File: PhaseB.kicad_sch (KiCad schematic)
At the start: 12 parts, among them Q10 Q_NMOS, Q9 Q_NMOS, U2 STDriveG600

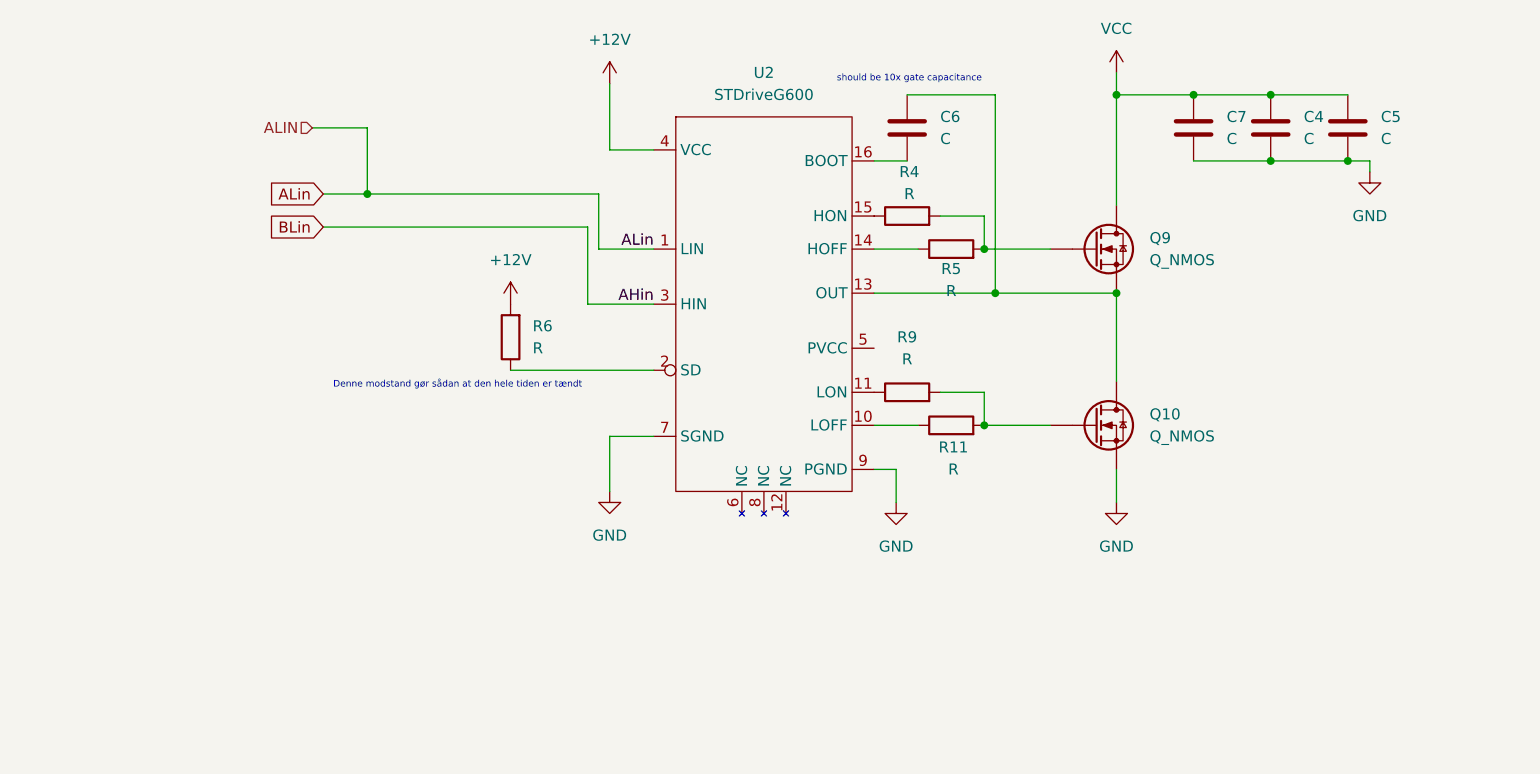
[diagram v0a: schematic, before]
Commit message: added hirearchical labels
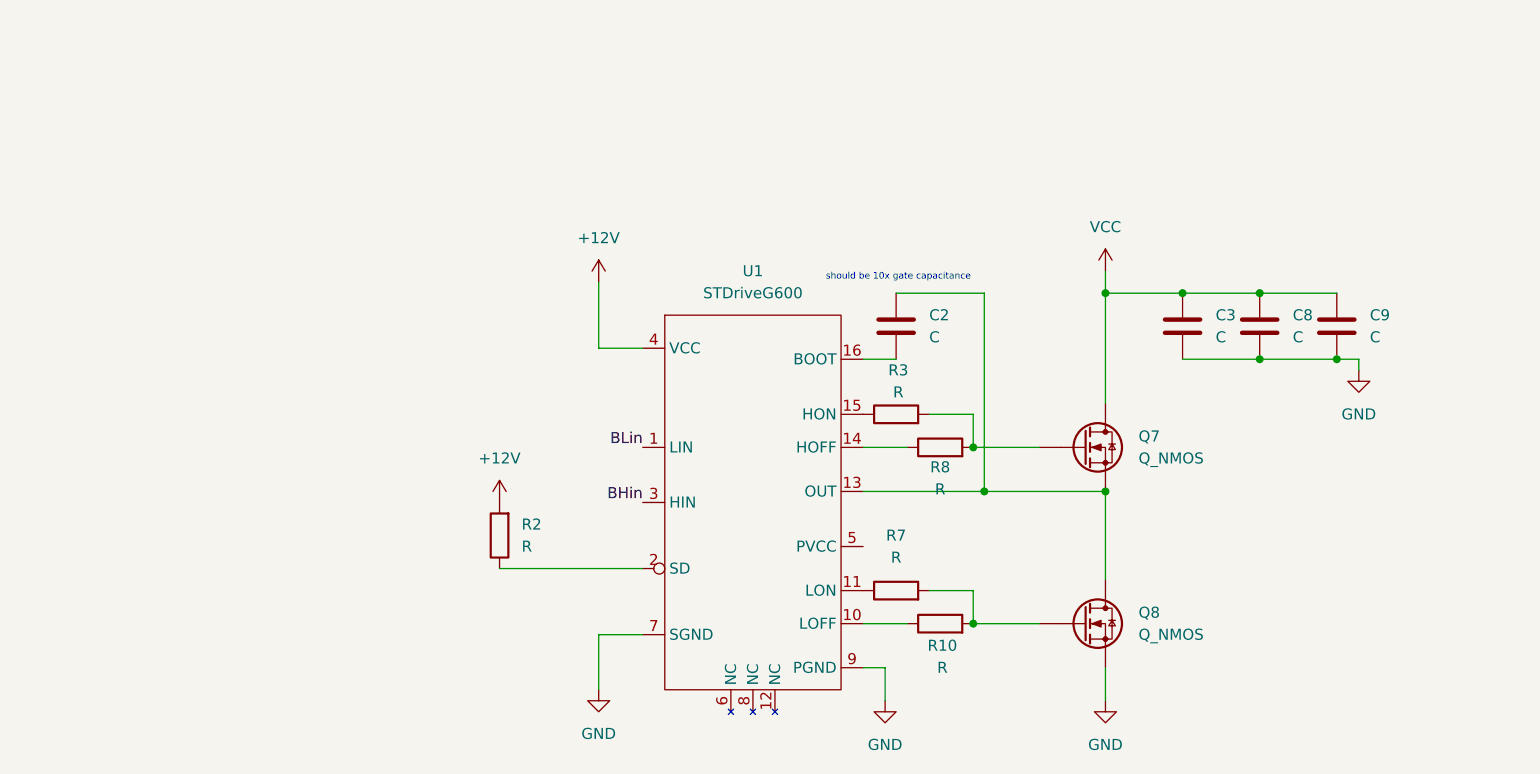
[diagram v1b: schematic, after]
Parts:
- removed C4, C5, C6, C7: C, symbol Device:C
- removed Q10, Q9: Q_NMOS, symbol Device:Q_NMOS
- removed R11, R4, R5, R6, R9: R, symbol Device:R
- removed U2: STDriveG600, Package_SO:SO-16_3.9x9.9mm_P1.27mm, symbol stm:STDRIVEG600
- added C2, C3, C8, C9: C, symbol Device:C
- added Q7, Q8: Q_NMOS, symbol Device:Q_NMOS
- added R10, R2, R3, R7, R8: R, symbol Device:R
- added U1: STDriveG600, Package_SO:SO-16_3.9x9.9mm_P1.27mm, symbol stm:STDRIVEG600
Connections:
- net +12V: now also R2.2, U1.4 (VCC)
- net BLin: now also U1.1 (LIN)
- net GND: now also C3.2, C8.2, C9.2, Q8.S, U1.7 (SGND), U1.9 (PGND)
- net VCC: now also C3.1, C8.1, C9.1, Q7.D
- new net: C2.1, Q7.S, Q8.D, U1.13 (OUT)
- new net: C2.2, U1.16 (BOOT)
- new net: R8.1, U1.14 (HOFF)
- new net: Q7.G, R3.2, R8.2
- new net: R10.1, U1.10 (LOFF)
- new net: R7.1, U1.11 (LON)
- new net: R3.1, U1.15 (HON)
- new net: R2.1, U1.2 (SD)
- new net: Q8.G, R10.2, R7.2
- new net BHin: U1.3 (HIN)
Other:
- note removed: "Denne modstand gør sådan at den hele tiden er tændt"

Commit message: added more data for the 3 Phases. also added transformer
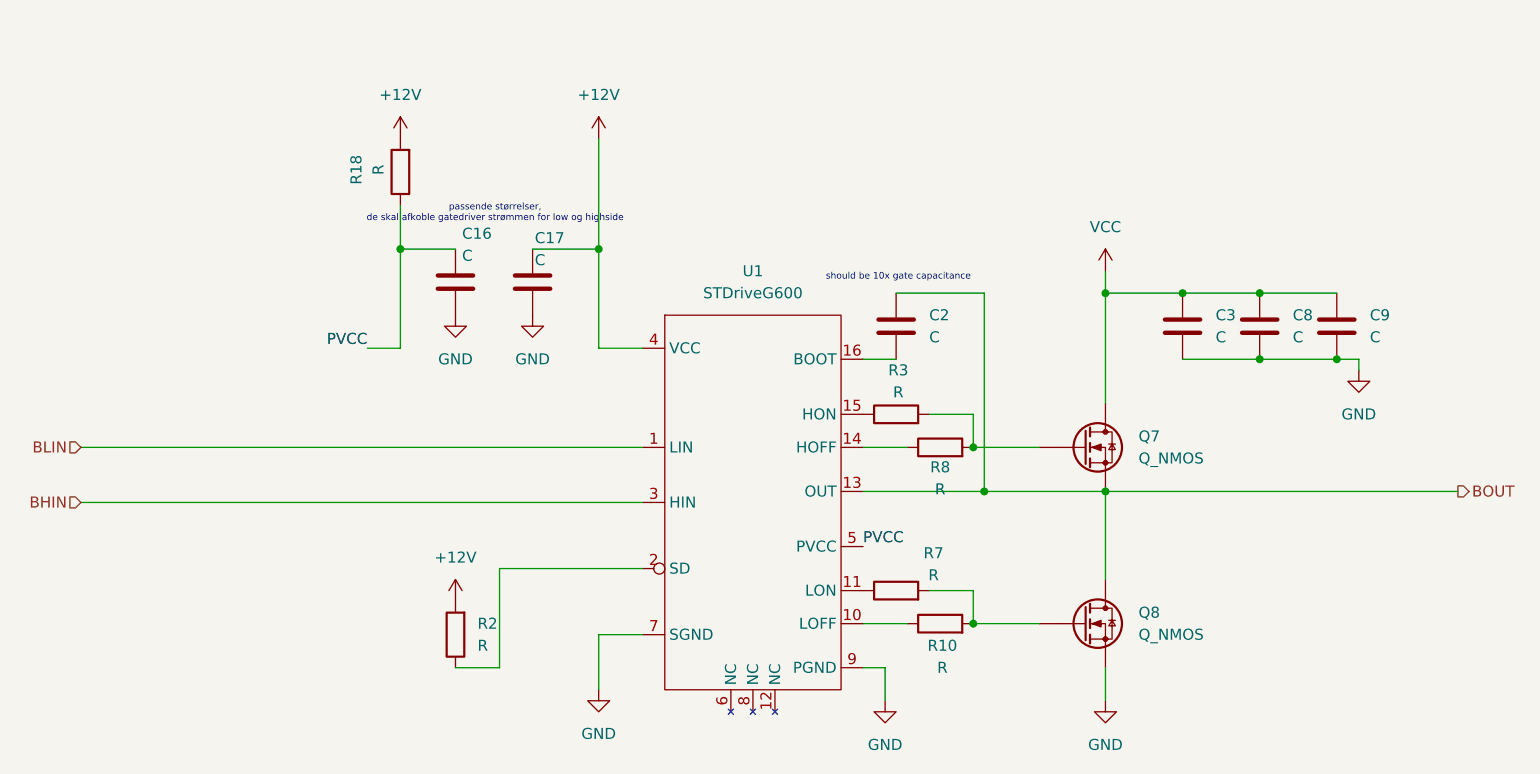
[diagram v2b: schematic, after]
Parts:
- added C16, C17: C, symbol Device:C
- added R18: R, symbol Device:R
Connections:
- net +12V: now also C17.1, R18.2
- net GND: now also C16.2, C17.2
- net BOUT: now reaches C2.1, Q7.S, Q8.D, U1.13 (OUT)
- net PVCC: now reaches U1.5 (PVCC)
- net PVCC: now also C16.1, R18.1
- net BHin renamed BHIN
- net BLin renamed BLIN
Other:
- note added: "passende størrelser, de skal afkoble gatedriver strømmen for low og highside"
- moved on the sheet: R2

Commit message: small changes
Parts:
- C16, C17, C3: value C -> 10u
- C2: value C -> 470n
- C8, C9: value C -> 100u
- R18: value R -> 3
- R2: value R -> 10k
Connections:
- net VCC renamed +48V
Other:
- note added: "flere typer kapacitorer husk strømvejen"
- note added: "should be 10x gate capacitance husk LAV ESR så nok MLCC X7R"
- note removed: "should be 10x gate capacitance"
- moved on the sheet: R2

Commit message: added some kind of PCB design, a rough draft
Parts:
- removed Q7, Q8: Q_NMOS, symbol Device:Q_NMOS
- added Q14, Q8: C2M0025120D, Package_TO_SOT_THT:TO-247-3_Vertical, symbol Transistor_FET:C2M0025120D
- C10: renamed from C2; footprint (none) -> Capacitor_SMD:C_1206_3216Metric
- C11: renamed from C3; footprint (none) -> Capacitor_SMD:C_2220_5750Metric
- C12: renamed from C8; footprint (none) -> Capacitor_SMD:C_Elec_6.3x7.7
- C13: renamed from C9; footprint (none) -> Capacitor_SMD:C_Elec_6.3x7.7
- C8: renamed from C16; footprint (none) -> Capacitor_SMD:C_1812_4532Metric
- C9: renamed from C17; footprint (none) -> Capacitor_SMD:C_1812_4532Metric
- R10: renamed from R8; footprint (none) -> Resistor_SMD:R_1206_3216Metric
- R11: renamed from R7; footprint (none) -> Resistor_SMD:R_1206_3216Metric
- R12: renamed from R2; footprint (none) -> Resistor_SMD:R_1812_4532Metric
- R13: renamed from R10; footprint (none) -> Resistor_SMD:R_1206_3216Metric
- R8: renamed from R18; footprint (none) -> Resistor_SMD:R_1210_3225Metric
- R9: renamed from R3; footprint (none) -> Resistor_SMD:R_1206_3216Metric
- renumbered U1 to U2
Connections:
- net +48V: now also Q8.2 (D)
- net BOUT: now also Q14.2 (D), Q8.3 (S)
- net GND: now also Q14.3 (S)
- net at R10.2, R9.2: now also Q8.1 (G)
- net at R11.2, R13.2: now also Q14.1 (G)

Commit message: intial pcb layout
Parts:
- Q14, Q8: footprint Package_TO_SOT_THT:TO-247-3_Vertical -> Package_TO_SOT_SMD:TO-252-2
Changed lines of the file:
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@@
 			)
 		)
-		(property "Footprint" "Package_TO_SOT_THT:TO-247-3_Vertical"
+		(property "Footprint" "Package_TO_SOT_SMD:TO-252-2"
 			(at 173.99 114.935 0)
 			(effects
@@
 			)
 		)
-		(property "Footprint" "Package_TO_SOT_THT:TO-247-3_Vertical"
+		(property "Footprint" "Package_TO_SOT_SMD:TO-252-2"
 			(at 173.99 94.615 0)
 			(effects

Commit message: local restore changes
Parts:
- C10: LCSC Part Number (none) -> C507059
- C11: LCSC Part Number (none) -> C2843466
- C12: value 100u -> 47u; footprint Capacitor_SMD:C_Elec_6.3x7.7 -> easyeda:CAP-SMD_BD6.3-L6.6-W6.6-LS7.3-FD; LCSC Part Number (none) -> C7461235
- C13: footprint Capacitor_SMD:C_Elec_6.3x7.7 -> easyeda:CAP-SMD_BD8.0-L8.3-W8.3-LS9.2-FD-H10.5; LCSC Part Number (none) -> C5456764
- C8, C9: LCSC Part Number (none) -> C1021609
- Q14, Q8, R10, R11, R13, R9: now left out of the parts list
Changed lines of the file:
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@@
+			)
+		)
+		(property "LCSC Part Number" "C2843466 "
+			(at 182.88 78.74 0)
+			(effects
+				(font
+					(size 1.27 1.27)
+				)
+				(hide yes)
 			)
 		)
@@
 			)
 		)
+		(property "LCSC Part Number" "C507059"
+			(at 147.32 78.74 0)
+			(effects
+				(font
+					(size 1.27 1.27)
+				)
+				(hide yes)
+			)
+		)
 		(pin "2"
 		)
@@
 		(unit 1)
 		(exclude_from_sim no)
-		(in_bom yes)
+		(in_bom no)
 		(on_board yes)
 		(dnp no)
@@
 		)
 		(property "Description" "Unpolarized capacitor"
+			(at 96.52 73.66 0)
+			(effects
+				(font
+					(size 1.27 1.27)
+				)
+				(hide yes)
+			)
+		)
+		(property "LCSC Part Number" "C1021609"
 			(at 96.52 73.66 0)
 			(effects
@@
 			)
 		)
-		(property "Value" "100u"
+		(property "Value" "47u"
 			(at 196.85 80.0099 0)
 			(effects
@@
 			)
 		)
-		(property "Footprint" "Capacitor_SMD:C_Elec_6.3x7.7"
+		(property "Footprint" "easyeda:CAP-SMD_BD6.3-L6.6-W6.6-LS7.3-FD"
 			(at 194.0052 82.55 0)
 			(effects
@@
 		)
 		(property "Description" "Unpolarized capacitor"
+			(at 193.04 78.74 0)
+			(effects
+				(font
+					(size 1.27 1.27)
+				)
+				(hide yes)
+			)
+		)
+		(property "LCSC Part Number" "C7461235"
 			(at 193.04 78.74 0)
 			(effects
@@
 			)
 		)
+		(property "LCSC Part Number" "C1021609"
+			(at 105.41 73.66 0)
+			(effects
+				(font
+					(size 1.27 1.27)
+				)
+				(hide yes)
+			)
+		)
 		(pin "2"
 		)
@@
 			)
 		)
-		(property "Footprint" "Capacitor_SMD:C_Elec_6.3x7.7"
+		(property "Footprint" "easyeda:CAP-SMD_BD8.0-L8.3-W8.3-LS9.2-FD-H10.5"
 			(at 205.4352 82.55 0)
 			(effects
@@
 			)
 		)
+		(property "LCSC Part Number" "C5456764"
+			(at 204.47 78.74 0)
+			(effects
+				(font
+					(size 1.27 1.27)
+				)
+				(hide yes)
+			)
+		)
 		(pin "1"
 		)
@@
 		(unit 1)
 		(exclude_from_sim no)
-		(in_bom yes)
+		(in_bom no)
 		(on_board yes)
 		(dnp no)
@@
 		(unit 1)
 		(exclude_from_sim no)
-		(in_bom yes)
+		(in_bom no)
 		(on_board yes)
 		(dnp no)
@@
 		(unit 1)
 		(exclude_from_sim no)
-		(in_bom yes)
+		(in_bom no)
 		(on_board yes)
 		(dnp no)
@@
 		(unit 1)
 		(exclude_from_sim no)
-		(in_bom yes)
+		(in_bom no)
 		(on_board yes)
 		(dnp no)
@@
 		(unit 1)
 		(exclude_from_sim no)
-		(in_bom yes)
-		(on_board yes)
-		(dnp no)
+		(in_bom no)
+		(on_board yes)
+		(dnp no)

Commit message: all små komponenter er nu 0805, og jeg har fixet strømmen under kondensatorerene, mangler kun at bytte rundt på 12Vin og GND
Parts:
- C10: footprint Capacitor_SMD:C_1206_3216Metric -> Capacitor_SMD:C_0805_2012Metric_Pad1.18x1.45mm_HandSolder
- C8, C9: footprint Capacitor_SMD:C_1812_4532Metric -> Capacitor_SMD:C_0805_2012Metric_Pad1.18x1.45mm_HandSolder
- R10, R11, R13, R9: footprint Resistor_SMD:R_1206_3216Metric -> Resistor_SMD:R_0805_2012Metric_Pad1.20x1.40mm_HandSolder
- R12: footprint Resistor_SMD:R_1812_4532Metric -> Resistor_SMD:R_0805_2012Metric_Pad1.20x1.40mm_HandSolder
- R8: footprint Resistor_SMD:R_1210_3225Metric -> Resistor_SMD:R_0805_2012Metric_Pad1.20x1.40mm_HandSolder
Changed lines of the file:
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@@
 			)
 		)
-		(property "Footprint" "Resistor_SMD:R_1210_3225Metric"
+		(property "Footprint" "Resistor_SMD:R_0805_2012Metric_Pad1.20x1.40mm_HandSolder"
 			(at 91.948 60.96 90)
 			(effects
@@
 			)
 		)
-		(property "Footprint" "Capacitor_SMD:C_1206_3216Metric"
+		(property "Footprint" "Capacitor_SMD:C_0805_2012Metric_Pad1.18x1.45mm_HandSolder"
 			(at 148.2852 82.55 0)
 			(effects
@@
 			)
 		)
-		(property "Footprint" "Resistor_SMD:R_1206_3216Metric"
+		(property "Footprint" "Resistor_SMD:R_0805_2012Metric_Pad1.20x1.40mm_HandSolder"
 			(at 152.4 94.488 90)
 			(effects
@@
 			)
 		)
-		(property "Footprint" "Capacitor_SMD:C_1812_4532Metric"
+		(property "Footprint" "Capacitor_SMD:C_0805_2012Metric_Pad1.18x1.45mm_HandSolder"
 			(at 97.4852 77.47 0)
 			(effects
@@
 			)
 		)
-		(property "Footprint" "Capacitor_SMD:C_1812_4532Metric"
+		(property "Footprint" "Capacitor_SMD:C_0805_2012Metric_Pad1.18x1.45mm_HandSolder"
 			(at 106.3752 77.47 0)
 			(effects
@@
 			)
 		)
-		(property "Footprint" "Resistor_SMD:R_1206_3216Metric"
+		(property "Footprint" "Resistor_SMD:R_0805_2012Metric_Pad1.20x1.40mm_HandSolder"
 			(at 152.4 114.808 90)
 			(effects
@@
 			)
 		)
-		(property "Footprint" "Resistor_SMD:R_1812_4532Metric"
+		(property "Footprint" "Resistor_SMD:R_0805_2012Metric_Pad1.20x1.40mm_HandSolder"
 			(at 88.138 113.03 90)
 			(effects
@@
 			)
 		)
-		(property "Footprint" "Resistor_SMD:R_1206_3216Metric"
+		(property "Footprint" "Resistor_SMD:R_0805_2012Metric_Pad1.20x1.40mm_HandSolder"
 			(at 147.32 90.678 90)
 			(effects
@@
 			)
 		)
-		(property "Footprint" "Resistor_SMD:R_1206_3216Metric"
+		(property "Footprint" "Resistor_SMD:R_0805_2012Metric_Pad1.20x1.40mm_HandSolder"
 			(at 147.32 110.998 90)
 			(effects

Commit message: Final Value Changes
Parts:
- Q14, Q8: value C2M0025120D -> FDD3672
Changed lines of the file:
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@@
 			)
 		)
-		(property "Value" "C2M0025120D"
+		(property "Value" "FDD3672"
 			(at 175.26 114.2999 0)
 			(effects
@@
 			)
 		)
-		(property "Datasheet" "https://www.wolfspeed.com/media/downloads/161/C2M0025120D.pdf"
+		(property "Datasheet" "https://www.onsemi.com/pdf/datasheet/fdd3672-d.pdf"
 			(at 173.99 116.84 0)
 			(effects
@@
 			)
 		)
-		(property "Description" "90A Id, 1200V Vds, 25mOhm, N-Channel SiC MOSFET, TO-247"
+		(property "Description" ""
 			(at 168.91 113.03 0)
 			(effects
@@
 			)
 		)
-		(property "Value" "C2M0025120D"
+		(property "Value" "FDD3672"
 			(at 175.26 93.9799 0)
 			(effects
@@
 			)
 		)
-		(property "Datasheet" "https://www.wolfspeed.com/media/downloads/161/C2M0025120D.pdf"
+		(property "Datasheet" "https://www.onsemi.com/pdf/datasheet/fdd3672-d.pdf"
 			(at 173.99 96.52 0)
 			(effects
@@
 			)
 		)
-		(property "Description" "90A Id, 1200V Vds, 25mOhm, N-Channel SiC MOSFET, TO-247"
+		(property "Description" ""
 			(at 168.91 92.71 0)
 			(effects
